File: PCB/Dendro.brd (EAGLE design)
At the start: 74.9 x 39.4 mm, 5 parts

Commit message: Dendro PCB V1.1
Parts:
- NEOPIXEL: value 455-1750-1-ND -> (none)
- moved SHT30D 31.5 mm to (38.2, 26.7), turned to 90 degrees
- moved MS1 26.6 mm to (1.14, -1.47)
- moved NEOPIXEL 25.0 mm to (29.2, 26.7), turned to 90 degrees
- moved BUTTON 23.4 mm to (19.1, 26.7), turned to 90 degrees
- moved AS5311 20.4 mm to (3.81, 30.5)
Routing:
- net 3VRAIL: track 66.6 -> 0.00 mm, vias 2 -> 0
- net D11: track 79.6 -> 14.0 mm
- net SCL: track 61.1 -> 13.7 mm
- net SDA: track 63.4 -> 17.2 mm, vias 1 -> 0
- net A2: track 11.4 -> 49.8 mm
- net CSN: track 61.6 -> 26.2 mm
- net SCLK: track 45.5 -> 43.4 mm
- net DO: track 38.4 -> 39.0 mm
- added copper zone on layer 16, net 3VRAIL
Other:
- board size 74.9 x 39.4 mm -> 52.1 x 45.7 mm
- board text added: "3V"
- board text added: "D11"
- board text added: "Dendrometer V1.1"
- board text added: "SCL"
- board text added: "SDA"
- board text removed: "3VRAIL"
- board text removed: "CLK"
- board text removed: "DATA"
- board text removed: "Dendrometer V1.0"

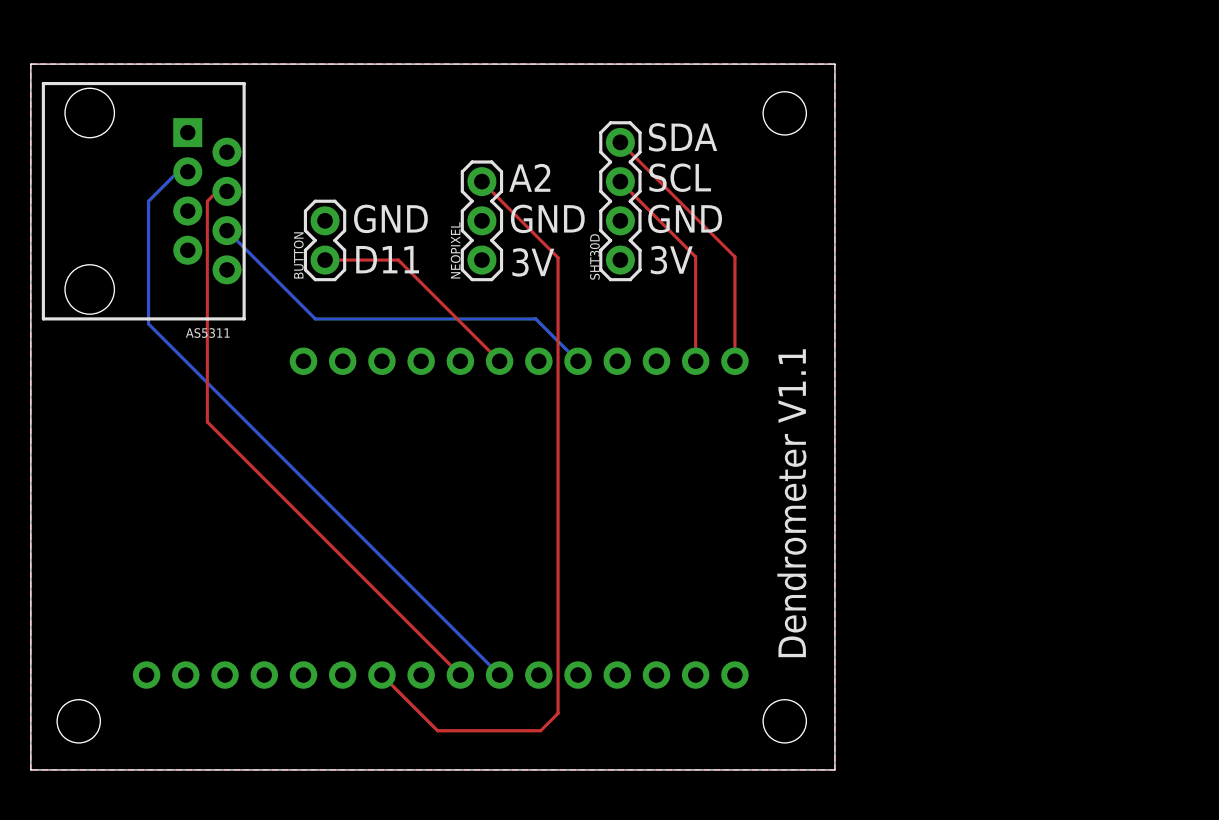
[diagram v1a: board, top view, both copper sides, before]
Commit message: Updated code + PCB for summer deployments
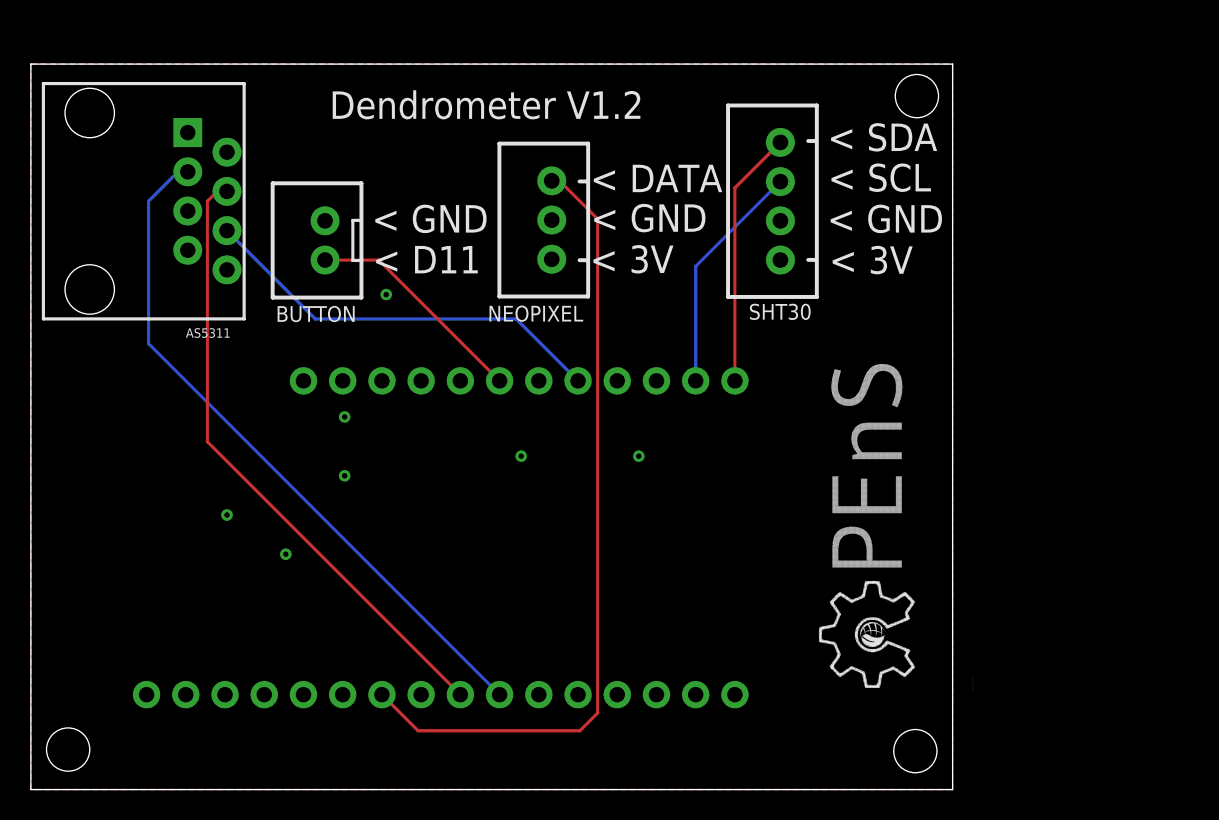
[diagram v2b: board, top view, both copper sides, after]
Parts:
- removed SHT30D: (no value), SparkFun-Connectors:1X04
- added SHT30: JST-XH-04-PIN-ROUND-PAD, Rembrandt Electronics - JST XH Connectors v1-0:JST-XH-04-PACKAGE-ROUND-PAD
- added U$1: (no value), opens-logo:OPENS-LOGO
- BUTTON: value (none) -> JST-XH-02-PIN-ROUND-PAD; device SparkFun-Connectors:1X02 -> Rembrandt Electronics - JST XH Connectors v1-0:JST-XH-02-PACKAGE-ROUND-PAD
- NEOPIXEL: value (none) -> JST-XH-03-PIN-ROUND-PAD; device SparkFun-Connectors:1X03 -> Rembrandt Electronics - JST XH Connectors v1-0:JST-XH-03-PACKAGE-ROUND-PAD
- moved NEOPIXEL 5.21 mm to (33.7, 29.3)
- moved MS1 1.27 mm to (1.14, -2.74)
- moved BUTTON 1.27 mm to (19.1, 27.9)
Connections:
- removed net 5VRAIL: MS1.26
- removed net VBAT: MS1.28
- net 3VRAIL: now also SHT30.1; no longer SHT30D.1
- net GND: now also SHT30.2; no longer SHT30D.2
- net SCL: now also SHT30.3; no longer SHT30D.3
- net SDA: now also SHT30.4; no longer SHT30D.4
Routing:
- net A2: track 49.8 -> 51.4 mm
- net SCL: track 13.7 -> 15.2 mm
- net DO: track 39.0 -> 40.3 mm
- net SCLK: track 43.4 -> 44.7 mm
- net SDA: track 17.2 -> 16.7 mm
- net D11: track 14.0 -> 14.5 mm
- net CSN: track 26.2 -> 26.8 mm
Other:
- board size 52.1 x 45.7 mm -> 59.7 x 47 mm
- board text added: "< 3V"
- board text added: "< D11"
- board text added: "< DATA"
- board text added: "< GND"
- board text added: "< SCL"
- board text added: "< SDA"
- board text added: "Dendrometer V1.2"
- board text removed: "3V"
- board text removed: "A2"
- board text removed: "D11"
- board text removed: "Dendrometer V1.1"
- board text removed: "GND"
- board text removed: "SCL"
- board text removed: "SDA"
